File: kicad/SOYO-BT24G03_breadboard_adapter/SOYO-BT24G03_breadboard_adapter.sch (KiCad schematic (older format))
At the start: 4 parts, among them J1 jack, P1 CONN_01X24, P2 CONN_01X23, U1 SOYO-BT24G03

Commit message: revork board to be only 25.4mm wide, for fit inside bread board and leave space for cables on both sides
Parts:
- removed P2: CONN_01X23, Pin_Headers:Pin_Header_Straight_1x23, symbol CONN_01X23
- added P2, P3, P4: CONN_01X24, Pin_Headers:Pin_Header_Straight_1x12, symbol CONN_01X12
- P1: footprint Pin_Headers:Pin_Header_Straight_1x24 -> Pin_Headers:Pin_Header_Straight_1x12; symbol CONN_01X24 -> CONN_01X12
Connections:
- net at U1.1 (IR_IN): now also P2.1 (P1); no longer P1.19 (P19)
- net at U1.10 (SSD_CLK): now also P1.5 (P5); no longer P1.10 (P10)
- net at U1.11 (SSD_CMD): now also P1.4 (P4); no longer P1.9 (P9)
- net at U1.12 (SDATA3): now also P1.3 (P3); no longer P1.8 (P8)
- net at U1.13 (SDATA2): now also P1.2 (P2); no longer P1.7 (P7)
- net at J1.1, U1.14 (GND), U1.21 (GND)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: now also P2.11 (P11), P4.12 (P12); no longer P1.14 (P14)
- net at U1.15 (RESET): now also P4.11 (P11); no longer P1.5 (P5)
- net at U1.16 (PWRKEY_IN): now also P4.10 (P10); no longer P1.4 (P4)
- net at U1.17 (ST_LED): now also P4.9 (P9); no longer P1.3 (P3)
- net at U1.18 (BT_LED): now also P4.8 (P8); no longer P1.2 (P2)
- net at U1.19 (HP_DECT): now also P4.7 (P7); no longer P1.1 (P1)
- net at U1.2 (CARD_DECT): now also P1.12 (P12); no longer P1.18 (P18)
- net at U1.20 (MUTE): now also P4.6 (P6)
- net at U1.23 (BAT): now also P4.5 (P5)
- net at U1.24 (AU_RCV_P): now also P4.4 (P4)
- net at U1.25 (AU_RCV_N): now also P4.3 (P3)
- net at U1.26 (CHG_IN): now also P3.12 (P12)
- net at U1.27 (KEYIN_N): now also P3.11 (P11)
- net at U1.28 (KEYIN_P): now also P3.10 (P10)
- net at U1.29 (KEYIN_SEN): now also P3.9 (P9)
- net at U1.3 (UART_RX): now also P1.11 (P11); no longer P1.17 (P17)
- net at U1.30 (GP_ADC_IN_0): now also P3.8 (P8)
- net at U1.31 (LINE_DECT): now also P3.7 (P7)
- net at U1.32 (LINE_IN_L): now also P3.6 (P6)
- net at U1.33 (LINE_IN_R): now also P3.5 (P5)
- net at J1.5, U1.34 (AU_HPL): now also P3.4 (P4)
- net at J1.2, U1.35 (AU_HPR): now also P3.3 (P3)
- net at U1.36 (AU_MIC_P): now also P3.2 (P2)
- net at U1.37 (AU_MIC_N): now also P3.1 (P1)
- net at U1.39 (FM_ANT): now also P2.12 (P12)
- net at U1.4 (UART_TX): now also P1.10 (P10); no longer P1.16 (P16)
- net at U1.41 (USB_DM): now also P2.10 (P10)
- net at U1.42 (USB_DP): now also P2.9 (P9)
- net at U1.43 (I2S_BCK): now also P2.8 (P8)
- net at U1.44 (I2S_IN): now also P2.7 (P7)
- net at U1.45 (I2S_DOUT): now also P2.6 (P6); no longer P1.24 (P24)
- net at U1.46 (I2S_LRCK): now also P2.5 (P5); no longer P1.23 (P23)
- net at U1.47 (HST_TXD): now also P2.4 (P4); no longer P1.22 (P22)
- net at U1.48 (HST_RXD): now also P2.3 (P3); no longer P1.21 (P21)
- net at U1.5 (V_MMC): now also P1.9 (P9); no longer P1.15 (P15)
- net at U1.50 (BT_ANT): now also P2.2 (P2); no longer P1.20 (P20)
- net at U1.51 (I2C2_SDA): now also P4.2 (P2)
- net at U1.52 (I2C2_SCL): now also P4.1 (P1)
- net at U1.53 (MCLK_26M): now also P1.1 (P1); no longer P1.6 (P6)
- net at U1.7 (V_PAD): now also P1.8 (P8); no longer P1.13 (P13)
- net at U1.8 (SDATA1): now also P1.7 (P7); no longer P1.12 (P12)
- net at U1.9 (SDATA0): now also P1.6 (P6); no longer P1.11 (P11)

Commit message: update pcb,jack, layout
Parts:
- J1: footprint jacks:3.5mm_stereo_jack_PJ306M -> jacks:PJ-327A
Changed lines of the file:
@@
 LIBS:contrib
 LIBS:valves
+LIBS:phonejack
 LIBS:SOYO-BT24G03
 LIBS:SOYO-BT24G03_breadboard_adapter-cache
@@
 F 0 "J1" H 8750 3950 60  0000 C CNN
 F 1 "jack" H 8750 3400 60  0000 C CNN
-F 2 "jacks:3.5mm_stereo_jack_PJ306M" H 8750 3650 60  0001 C CNN
+F 2 "jacks:PJ-327A" H 8750 3650 60  0001 C CNN
 F 3 "" H 8750 3650 60  0000 C CNN
 	1    8750 3650

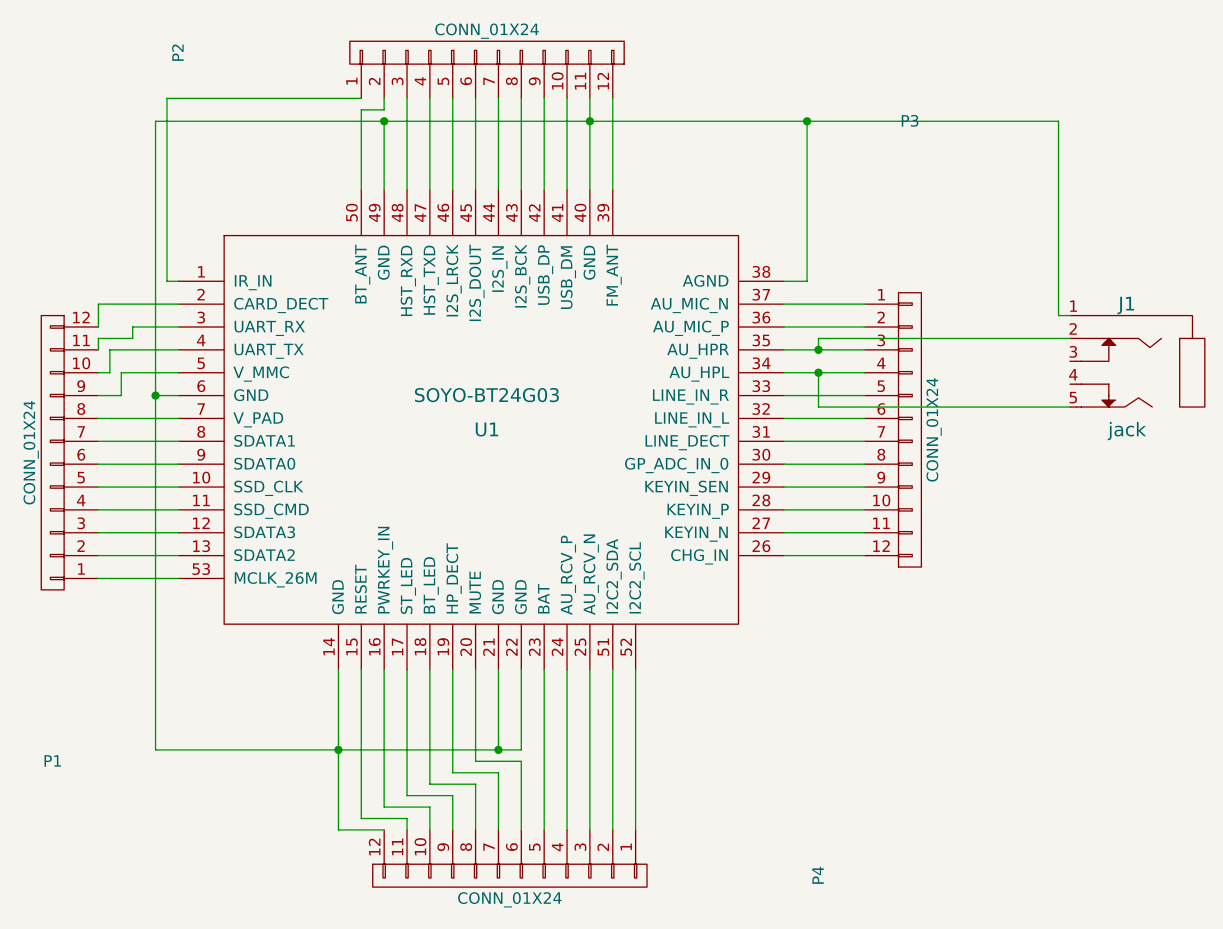
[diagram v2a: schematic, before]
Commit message: AGND pin separated from GND
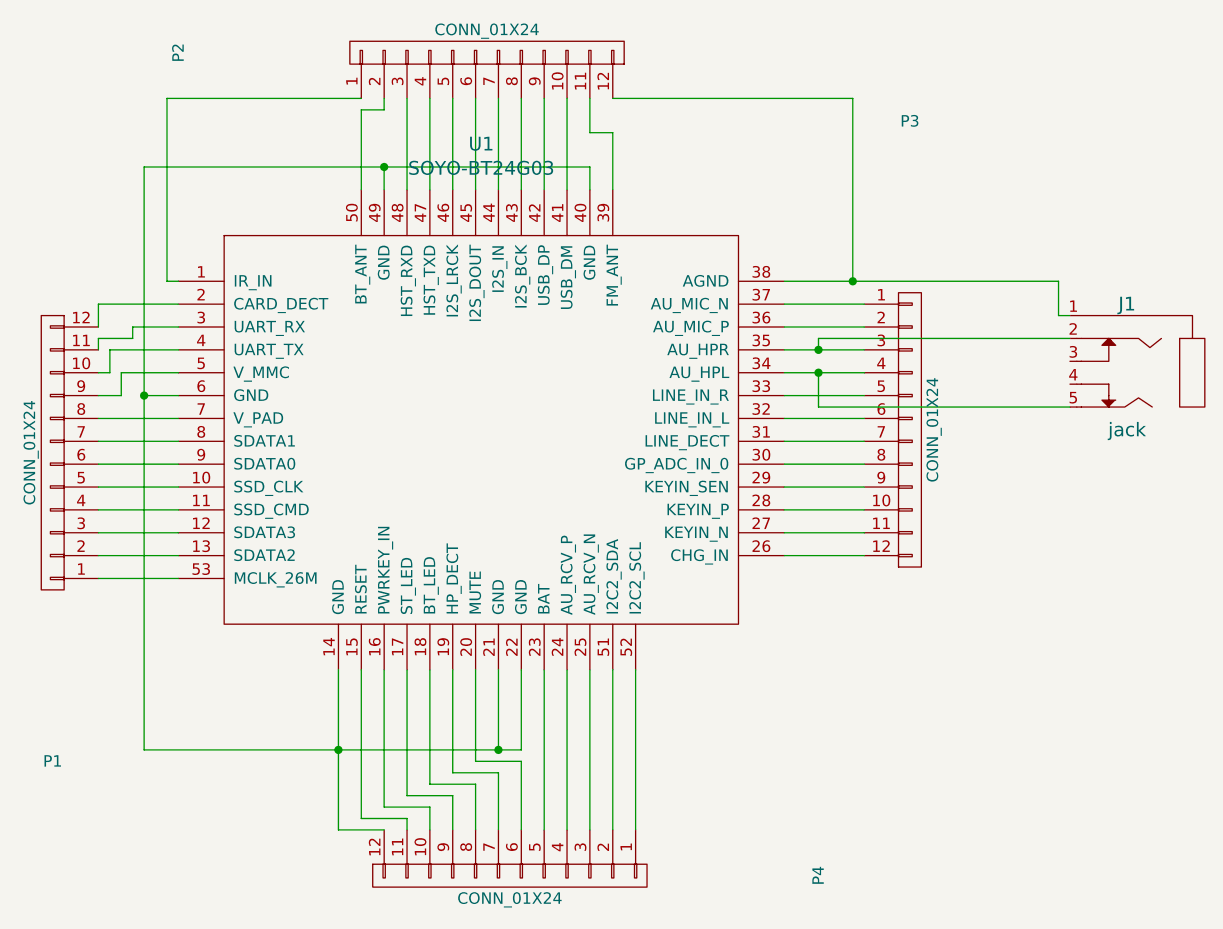
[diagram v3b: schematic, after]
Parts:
- U1: footprint my_modules:SOYO-BT24G03 -> (none)
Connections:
- net at P4.12 (P12), U1.14 (GND), U1.21 (GND)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: no longer J1.1, P2.11 (P11), U1.38 (AGND)
- net at P2.12 (P12): now also J1.1, U1.38 (AGND); no longer U1.39 (FM_ANT)
- new net: P2.11 (P11), U1.39 (FM_ANT)
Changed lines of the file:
@@
 EESchema Schematic File Version 2
+LIBS:SOYO-BT24G03_breadboard_adapter-rescue
 LIBS:power
 LIBS:device
@@
 $EndComp
 $Comp
-L SOYO-BT24G03 U1
-U 1 1 55EEB2F0
-P 5200 3800
-F 0 "U1" H 5950 3700 60  0000 C CNN
-F 1 "SOYO-BT24G03" H 5950 3850 60  0000 C CNN
-F 2 "my_modules:SOYO-BT24G03" H 5250 3800 60  0001 C CNN
-F 3 "" H 5250 3800 60  0000 C CNN
-	1    5200 3800
-	1    0    0    -1
-$EndComp
-$Comp
 L SCJ368R1NUS0B00G J1
 U 1 1 55EEE911
@@
 	5400 2500 5400 2850
 Wire Wire Line
-	6500 2450 6500 2850
-Wire Wire Line
 	7250 3850 7600 3850
 Wire Wire Line
@@
 	5700 4950 5700 5450
 Wire Wire Line
-	6400 2450 6400 2850
-Wire Wire Line
-	5500 2550 5500 2850
-Connection ~ 6400 2550
-Wire Wire Line
-	4500 2550 4500 5300
-Connection ~ 4500 3750
-Connection ~ 5500 2550
-Wire Wire Line
-	4500 5300 6100 5300
+	4450 5300 6100 5300
 Wire Wire Line
 	5300 4950 5300 5650
@@
 	5800 4950 5800 5400
 Wire Wire Line
-	8450 2550 8450 3400
-Wire Wire Line
 	8450 3400 8500 3400
 Wire Wire Line
@@
 Connection ~ 7400 3650
 Wire Wire Line
-	7350 3250 7350 2550
-Connection ~ 7350 2550
-Wire Wire Line
-	7350 3250 7250 3250
+	7250 3250 8450 3250
 Wire Wire Line
 	6100 5350 6100 5650
@@
 	4250 3450 4250 3350
 Wire Wire Line
-	4600 3750 4500 3750
-Wire Wire Line
 	4600 3250 4550 3250
 Wire Wire Line
@@
 	5500 2500 5400 2500
 Wire Wire Line
-	4500 2550 8450 2550
-Wire Wire Line
 	6000 2450 6000 2850
+Wire Wire Line
+	6400 2750 6400 2850
+Wire Wire Line
+	4450 2750 6400 2750
+Wire Wire Line
+	5500 2750 5500 2850
+Wire Wire Line
+	4450 3750 4600 3750
+Wire Wire Line
+	4450 2750 4450 5300
+Connection ~ 5500 2750
+Connection ~ 4450 3750
+Wire Wire Line
+	8450 3250 8450 3400
+$Comp
+L SOYO-BT24G03 U1
+U 1 1 57E8C39E
+P 5200 3800
+F 0 "U1" H 5925 4950 60  0000 C CNN
+F 1 "SOYO-BT24G03" H 5925 4844 60  0000 C CNN
+F 2 "" H 5250 3800 60  0000 C CNN
+F 3 "" H 5250 3800 60  0000 C CNN
+	1    5200 3800
+	1    0    0    -1
+$EndComp
+Wire Wire Line
+	6500 2850 6500 2600
+Wire Wire Line
+	6500 2600 6400 2600
+Wire Wire Line
+	6400 2600 6400 2450
+Wire Wire Line
+	6500 2450 7550 2450
+Wire Wire Line
+	7550 2450 7550 3250
+Connection ~ 7550 3250
 $EndSCHEMATC
